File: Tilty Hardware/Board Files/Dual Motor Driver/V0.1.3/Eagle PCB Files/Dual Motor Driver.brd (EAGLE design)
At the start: 38.4 x 50.8 mm, 42 parts, among them J1 AVR_SPI_PRG_62X3_LOCK, Q1 16MHz, U1 ATMEGA328P, U2 L298_BRIDGE_DRIVER, U3 LM2931

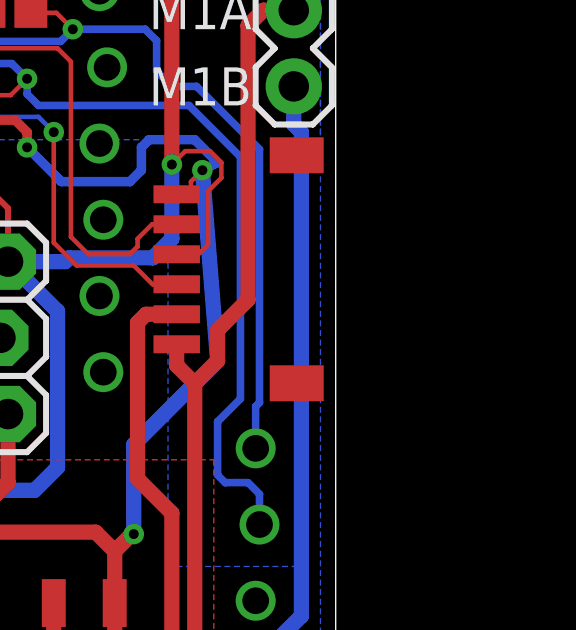
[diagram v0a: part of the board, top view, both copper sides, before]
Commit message: Added solder jumper to disable I2C level translation
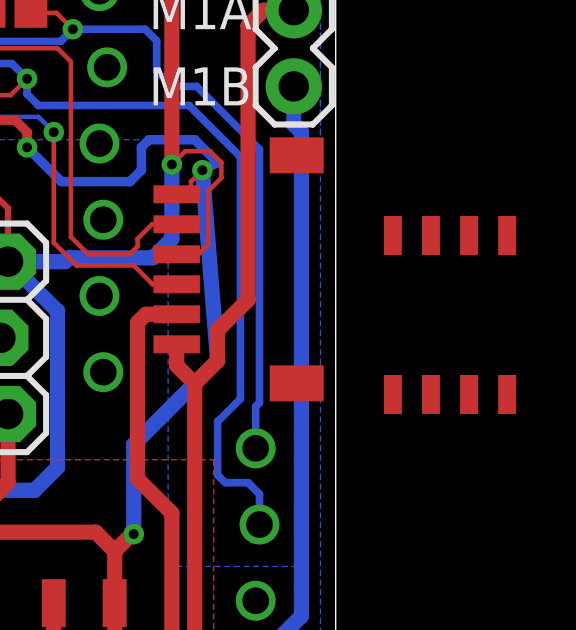
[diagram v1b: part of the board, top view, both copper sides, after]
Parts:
- added U$1: PCA9306, My Parts:SOIC-8
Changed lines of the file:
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@@
 <attribute name="VALUE" x="5.588" y="5.08" size="1.27" layer="27"/>
 </element>
+<element name="U$1" library="My Parts" package="SOIC-8" value="PCA9306" x="42.164" y="33.528" rot="R90"/>
 </elements>
 <signals>

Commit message: Updated RC adapter things.todo
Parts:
- moved U$1 1.55 mm to (40.6, 33.8)
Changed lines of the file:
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@@
 <attribute name="VALUE" x="5.588" y="5.08" size="1.27" layer="27"/>
 </element>
-<element name="U$1" library="My Parts" package="SOIC-8" value="PCA9306" x="42.164" y="33.528" rot="R90"/>
+<element name="U$1" library="My Parts" package="SOIC-8" value="PCA9306" x="40.64" y="33.782" rot="R90"/>
 </elements>
 <signals>

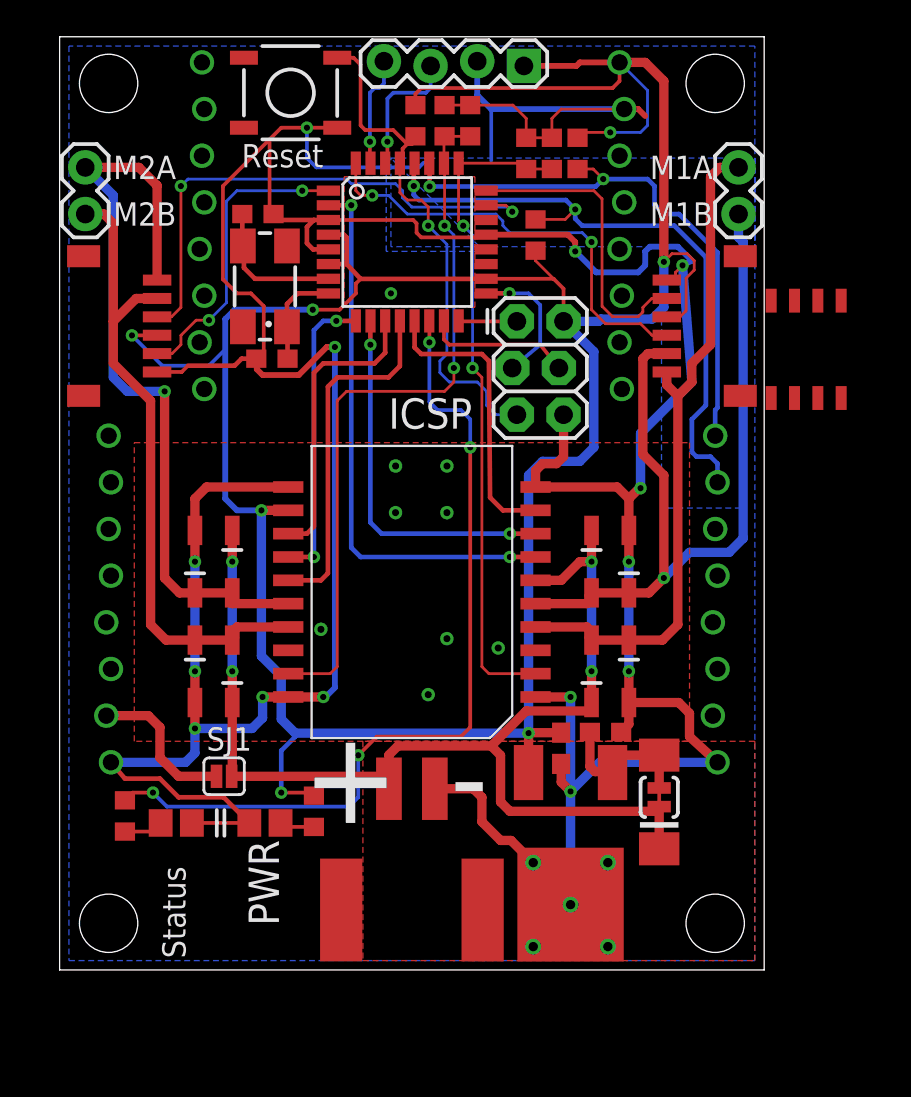
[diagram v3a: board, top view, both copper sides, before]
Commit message: Minor Dual Motor Driver Changes
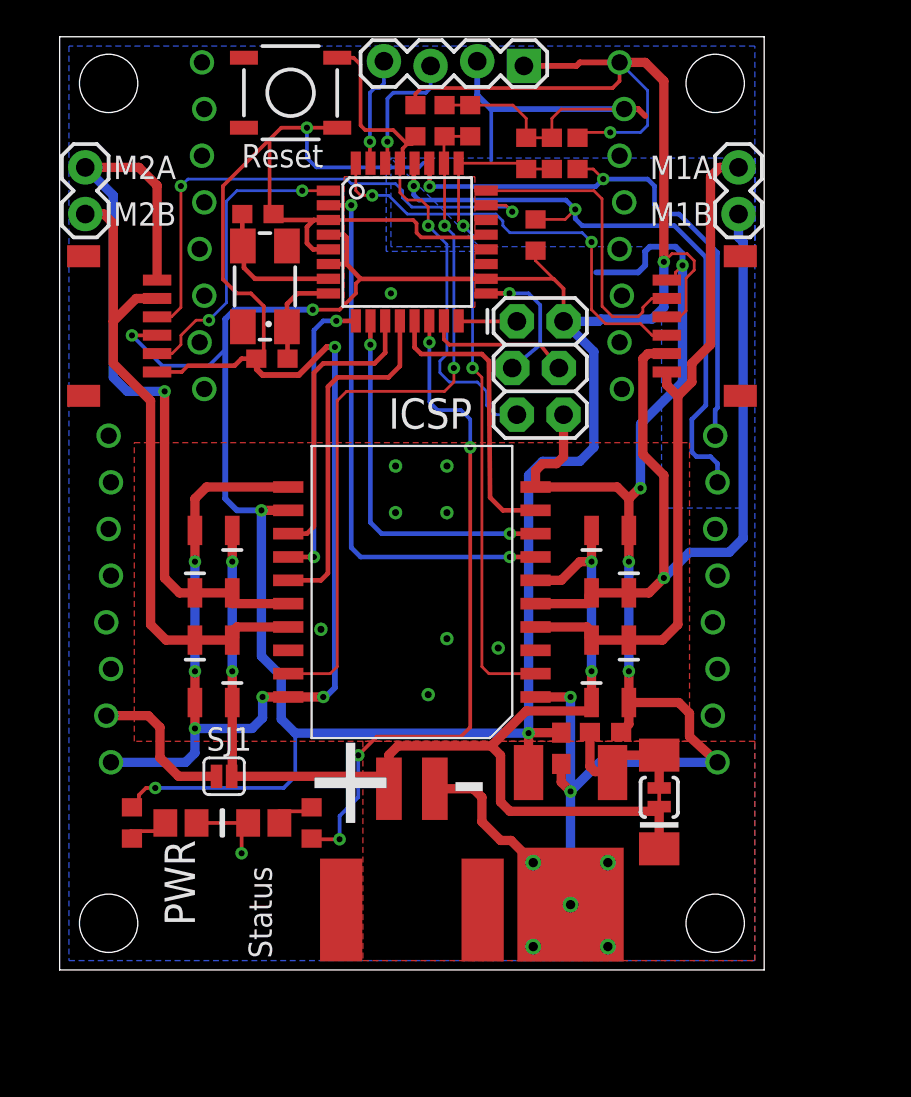
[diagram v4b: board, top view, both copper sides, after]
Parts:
- removed U$1: PCA9306, My Parts:SOIC-8
- moved R9 10.2 mm to (13.7, 8.00), turned to 90 degrees
- moved R6 9.93 mm to (3.94, 8.00)
- moved D11 4.76 mm to (11.1, 8.00), turned to 180 degrees
- moved D10 4.57 mm to (6.60, 8.00), turned to 0 degrees
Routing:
- net GND: track 256.3 -> 240.8 mm
- net N$4: track 46.2 -> 37.1 mm
- net +5V: track 166.2 -> 172.9 mm
- net N$1: track 1.91 -> 2.52 mm

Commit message: Connector changes to dual motor driver
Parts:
- removed D9: (no value), diode:DO214AA
- removed JP10: (no value), SparkFun-Connectors:1X02
- removed SJ2: (no value), SparkFun-Passives:SJ_2S-TRACE
- JP5: value 6PIN-SH_RIGHT_ANGLE -> 6-PIN-CONNECTORLEFT-MOTOR-JST; device con-jst:6PIN-SH_SERIES_RA -> My Parts:MOTOR-JST-6-PTH-LEFT
- JP6: value 6PIN-SH_RIGHT_ANGLE -> 6-PIN-CONNECTORRIGHT-MOTOR-JST; device con-jst:6PIN-SH_SERIES_RA -> My Parts:MOTOR-JST-6-PTH-RIGHT
- JP9: device SparkFun-Connectors:1X02 -> SparkFun-Connectors:1X08
- SJ1: value SOLDERJUMPERNC -> SOLDERJUMPERTRACE; device SparkFun-Passives:SJ_2S -> SparkFun-Passives:SJ_2S-TRACE
- moved JP9 57.5 mm to (0.76, -3.56), turned to 0 degrees
- moved JP6 3.70 mm to (36.4, 38.5), turned to 270 degrees
- moved JP5 3.36 mm to (2.29, 38.3), turned to 90 degrees
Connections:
- removed net N$3: C7.1, D9.A, SJ2.1, U3.P$2
- net +24V: now also C7.1, U3.P$2; no longer D9.C, SJ2.2
- net +5V: now also JP5.3, JP6.3; no longer JP5.P$4, JP6.P$4
- net ENC1A: now also JP6.4; no longer JP6.P$3
- net ENC1B: now also JP6.2; no longer JP6.P$5
- net ENC2A: now also JP5.4; no longer JP5.P$3
- net ENC2B: now also JP5.2; no longer JP5.P$5
- net GND: now also JP5.1, JP6.1; no longer JP5.P$6, JP6.P$6
- net M1A: now also JP6.6; no longer JP6.P$1, JP9.2
- net M1B: now also JP6.5; no longer JP6.P$2, JP9.1
- net M2A: now also JP5.6; no longer JP10.2, JP5.P$1
- net M2B: now also JP5.5; no longer JP10.1, JP5.P$2
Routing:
- net M2A: track 42.6 -> 30.4 mm
- net +24V: track 64.4 -> 55.2 mm
- net +5V: track 172.9 -> 164.2 mm
- net N$3: track 8.52 -> 0.00 mm
- net M2B: track 35.7 -> 30.5 mm
- net ENC2A: track 28.8 -> 24.0 mm, vias 2 -> 1
- net GND: track 240.8 -> 237.6 mm
- net M1B: track 44.6 -> 42.3 mm
- net ENC2B: track 16.5 -> 14.4 mm, vias 2 -> 1
- net M1A: track 37.1 -> 35.3 mm
- net ENC1B: track 16.7 -> 15.9 mm
- net ENC1A: track 24.0 -> 23.2 mm

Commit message: Removed redundant Motor Driver backups, changed power connector, and added reverse polarity diode
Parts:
- removed JP9: (no value), SparkFun-Connectors:1X08
- added D9: (no value), SparkFun-DiscreteSemi:SMB-DIODE
- added SJ2: SOLDERJUMPERNO, SparkFun-Passives:SJ_2S-NO
- JP7: value 2-POS_SMD_TERM_BLOCK -> (none); device My Parts:2-POS_SMD_TERMINAL_BLOCK -> SparkFun-Connectors:1X02
- moved JP7 3.05 mm to (19.2, 2.54), turned to 180 degrees
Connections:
- new net VIN: D9.A, JP7.2, SJ1.2, SJ2.1
- net +24V: now also D9.C, SJ2.2; no longer JP7.P$3, SJ1.2
- net GND: now also JP7.1; no longer JP7.P$4
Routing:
- net VIN: track 0.00 -> 18.1 mm
- net +24V: track 55.2 -> 62.0 mm
- net GND: track 237.6 -> 232.1 mm
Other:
- board text added: "Vin"
- board text removed: "+"
- board text removed: "-"
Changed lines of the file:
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@@
 <text x="0.508" y="40.894" size="1.27" layer="25" ratio="10">M2B</text>
 <text x="0.5715" y="42.926" size="1.27" layer="25" ratio="10">M2A</text>
-<text x="13.208" y="8.001" size="5.08" layer="25" ratio="10">+</text>
-<text x="21.2725" y="8.255" size="4.572" layer="25" ratio="10">-</text>
 <text x="8.001" y="11.938" size="1.27" layer="25" ratio="15">SJ1</text>
 <text x="9.906" y="43.688" size="1.27" layer="25" ratio="10">Reset</text>
@@
 <wire x1="30.48" y1="16.891" x2="31.496" y2="16.891" width="0.2032" layer="25"/>
 <text x="24.384" y="11.176" size="1.524" layer="26" ratio="12" rot="MR0">v0.1.2</text>
+<text x="14.986" y="0.508" size="1.524" layer="25" ratio="15" rot="R90">Vin</text>
+<text x="22.352" y="0.508" size="1.524" layer="25" ratio="15" rot="R90">GND</text>
 </plain>
 <attributes>
@@
 <attribute name="VALUE" x="30.988" y="13.97" size="1.27" layer="27" rot="R180"/>
 </element>
-<element name="JP7" library="My Parts" package="2-POS_SMD_TERMINAL_BLOCK" value="2-POS_SMD_TERM_BLOCK" x="19.177" y="5.588"/>
 <element name="JP8" library="SparkFun-Connectors" package="1X04_LOCK" value="" x="25.273" y="49.3395" smashed="yes" rot="R180">
 <attribute name="VALUE" x="26.543" y="52.5145" size="1.27" layer="27" rot="R180"/>
@@
 <element name="JP5" library="My Parts" package="MOTOR-JST-6-PTH-LEFT" value="6-PIN-CONNECTORLEFT-MOTOR-JST" x="2.286" y="38.2905" rot="R90"/>
 <element name="JP6" library="My Parts" package="MOTOR-JST-6-PTH-RIGHT" value="6-PIN-CONNECTORRIGHT-MOTOR-JST" x="36.3855" y="38.5445" rot="R270"/>
-<element name="JP9" library="SparkFun-Connectors" package="1X08" value="" x="0.762" y="-3.556"/>
+<element name="JP7" library="SparkFun-Connectors" package="1X02" value="" x="19.177" y="2.54" smashed="yes" rot="R180">
+<attribute name="VALUE" x="20.447" y="5.715" size="1.27" layer="27" rot="R180"/>
+</element>
+<element name="D9" library="SparkFun-DiscreteSemi" package="SMB-DIODE" value="" x="19.812" y="8.382" smashed="yes" rot="R180">
+<attribute name="VALUE" x="21.717" y="11.811" size="1.27" layer="27" rot="R180"/>
+<attribute name="PART#" value="SK24-TP" x="19.812" y="8.382" size="1.524" layer="27" ratio="15" rot="R180" display="off"/>
+</element>
+<element name="SJ2" library="SparkFun-Passives" package="SJ_2S-NO" value="SOLDERJUMPERNO" x="18.288" y="5.08" smashed="yes" rot="R90">
+<attribute name="VALUE" x="19.939" y="4.172" size="0.4064" layer="27" rot="R90"/>
+</element>
 </elements>
 <signals>
@@
 <contactref element="R3" pad="1"/>
 <contactref element="U3" pad="P$1"/>
-<contactref element="JP7" pad="P$4"/>
 <wire x1="14.6304" y1="40.824" x2="13.843" y2="40.824" width="0.254" layer="1"/>
 <wire x1="13.843" y1="40.824" x2="11.842" y2="40.824" width="0.254" layer="1"/>
@@
 <wire x1="13.462" y1="39.5605" x2="13.462" y2="40.443" width="0.254" layer="1"/>
 <wire x1="13.462" y1="40.443" x2="13.843" y2="40.824" width="0.254" layer="1"/>
-<wire x1="20.427" y1="9.863" x2="22.522" y2="9.863" width="0.508" layer="1"/>
-<wire x1="22.522" y1="9.863" x2="22.987" y2="9.398" width="0.508" layer="1"/>
-<wire x1="22.987" y1="9.398" x2="22.987" y2="8.0645" width="0.508" layer="1"/>
-<wire x1="22.987" y1="8.0645" x2="24.003" y2="7.0485" width="0.508" layer="1"/>
 <wire x1="24.003" y1="7.0485" x2="24.5745" y2="7.0485" width="0.508" layer="1"/>
 <wire x1="24.5745" y1="7.0485" x2="25.273" y2="6.35" width="0.508" layer="1"/>
@@
 <contactref element="JP5" pad="1"/>
 <contactref element="JP6" pad="1"/>
+<contactref element="JP7" pad="1"/>
 </signal>
 <signal name="M1A">
@@
 <contactref element="D7" pad="1"/>
 <contactref element="D8" pad="1"/>
-<contactref element="SJ1" pad="2"/>
 <via x="9.398" y="16.256" extent="1-16" drill="0.3302"/>
 <via x="9.398" y="22.225" extent="1-16" drill="0.3302"/>
@@
 <wire x1="28.956" y1="16.256" x2="28.956" y2="14.556" width="0.508" layer="1"/>
 <wire x1="28.956" y1="22.225" x2="28.956" y2="23.925" width="0.508" layer="1"/>
-<contactref element="JP7" pad="P$3"/>
-<wire x1="17.927" y1="9.863" x2="17.927" y2="10.5845" width="0.508" layer="1"/>
-<wire x1="17.927" y1="11.704" x2="18.415" y2="12.192" width="0.508" layer="1"/>
-<wire x1="18.415" y1="12.192" x2="23.495" y2="12.192" width="0.508" layer="1"/>
 <wire x1="28.956" y1="14.556" x2="28.956" y2="14.097" width="0.508" layer="1"/>
-<wire x1="23.495" y1="12.192" x2="25.4" y2="14.097" width="0.508" layer="1"/>
+<wire x1="22.9235" y1="11.6205" x2="25.4" y2="14.097" width="0.508" layer="1"/>
 <wire x1="28.956" y1="22.225" x2="28.321" y2="22.225" width="0.508" layer="1"/>
 <wire x1="28.321" y1="22.225" x2="27.305" y2="21.209" width="0.508" layer="1"/>
 <wire x1="27.305" y1="21.209" x2="25.908" y2="21.209" width="0.508" layer="1"/>
-<wire x1="9.398" y1="14.556" x2="9.398" y2="10.5736" width="0.508" layer="1"/>
-<wire x1="9.398" y1="10.5736" x2="9.4615" y2="10.541" width="0.508" layer="1"/>
-<wire x1="17.927" y1="11.704" x2="17.927" y2="10.5845" width="0.508" layer="1"/>
-<wire x1="17.927" y1="10.5845" x2="17.9705" y2="10.541" width="0.508" layer="1"/>
-<wire x1="17.9705" y1="10.541" x2="9.4615" y2="10.541" width="0.508" layer="1"/>
 <wire x1="25.4" y1="14.097" x2="28.956" y2="14.097" width="0.508" layer="1"/>
 <wire x1="28.956" y1="14.097" x2="29.0195" y2="14.0335" width="0.508" layer="1"/>
@@
 <wire x1="29.0195" y1="14.0335" x2="28.868" y2="14.0335" width="0.508" layer="1"/>
 <wire x1="28.868" y1="14.0335" x2="28.868" y2="12.954" width="0.508" layer="1"/>
+<contactref element="D9" pad="C"/>
+<wire x1="22.9235" y1="11.6205" x2="22.9235" y2="8.7855" width="0.508" layer="1"/>
+<wire x1="22.9235" y1="8.7855" x2="22.012" y2="8.382" width="0.508" layer="1"/>
+<wire x1="9.398" y1="14.556" x2="9.398" y2="12.7" width="0.508" layer="1"/>
+<wire x1="9.398" y1="12.7" x2="9.906" y2="12.192" width="0.508" layer="1"/>
+<wire x1="9.906" y1="12.192" x2="14.224" y2="12.192" width="0.508" layer="1"/>
+<wire x1="14.224" y1="12.192" x2="16.002" y2="10.414" width="0.508" layer="1"/>
+<wire x1="16.002" y1="10.414" x2="21.717" y2="10.414" width="0.508" layer="1"/>
+<wire x1="21.717" y1="10.414" x2="22.9235" y2="11.6205" width="0.508" layer="1"/>
+<contactref element="SJ2" pad="2"/>
+<wire x1="18.288" y1="5.53" x2="20.262" y2="5.53" width="0.508" layer="1"/>
+<wire x1="20.262" y1="5.53" x2="21.082" y2="6.35" width="0.508" layer="1"/>
+<wire x1="21.082" y1="6.35" x2="21.082" y2="7.452" width="0.508" layer="1"/>
+<wire x1="21.082" y1="7.452" x2="22.012" y2="8.382" width="0.508" layer="1"/>
 </signal>
 <signal name="+5V">
@@
 <wire x1="13.755" y1="7.112" x2="13.716" y2="7.151" width="0.2032" layer="1"/>
 </signal>
+<signal name="VIN">
+<contactref element="JP7" pad="2"/>
+<contactref element="D9" pad="A"/>
+<contactref element="SJ1" pad="2"/>
+<wire x1="9.4615" y1="10.541" x2="14.605" y2="10.541" width="0.508" layer="1"/>
+<wire x1="16.723" y1="8.763" x2="17.612" y2="8.382" width="0.508" layer="1"/>
+<contactref element="SJ2" pad="1"/>
+<wire x1="16.637" y1="2.54" x2="16.637" y2="4.064" width="0.508" layer="1"/>
+<wire x1="16.637" y1="4.064" x2="16.637" y2="7.407" width="0.508" layer="1"/>
+<wire x1="16.637" y1="7.407" x2="17.612" y2="8.382" width="0.508" layer="1"/>
+<wire x1="14.605" y1="10.541" x2="15.875" y2="9.271" width="0.508" layer="1"/>
+<wire x1="15.875" y1="9.271" x2="16.723" y2="9.271" width="0.508" layer="1"/>
+<wire x1="16.723" y1="9.271" x2="17.612" y2="8.382" width="0.508" layer="1"/>
+<wire x1="18.288" y1="4.63" x2="17.203" y2="4.63" width="0.508" layer="1"/>
+<wire x1="17.203" y1="4.63" x2="16.637" y2="4.064" width="0.508" layer="1"/>
+</signal>
 </signals>
